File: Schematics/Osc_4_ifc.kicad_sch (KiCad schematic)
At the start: 34 parts, among them J35 Conn_01x10h, J37 Conn_01x12, J39 Conn_01x10h, J41 Conn_01x12, P2 Conn_01x03, U20 LM324, U85 LMT358N, U86 LM358, U87 LM358, U88 LMT358N, U97 LM78L05

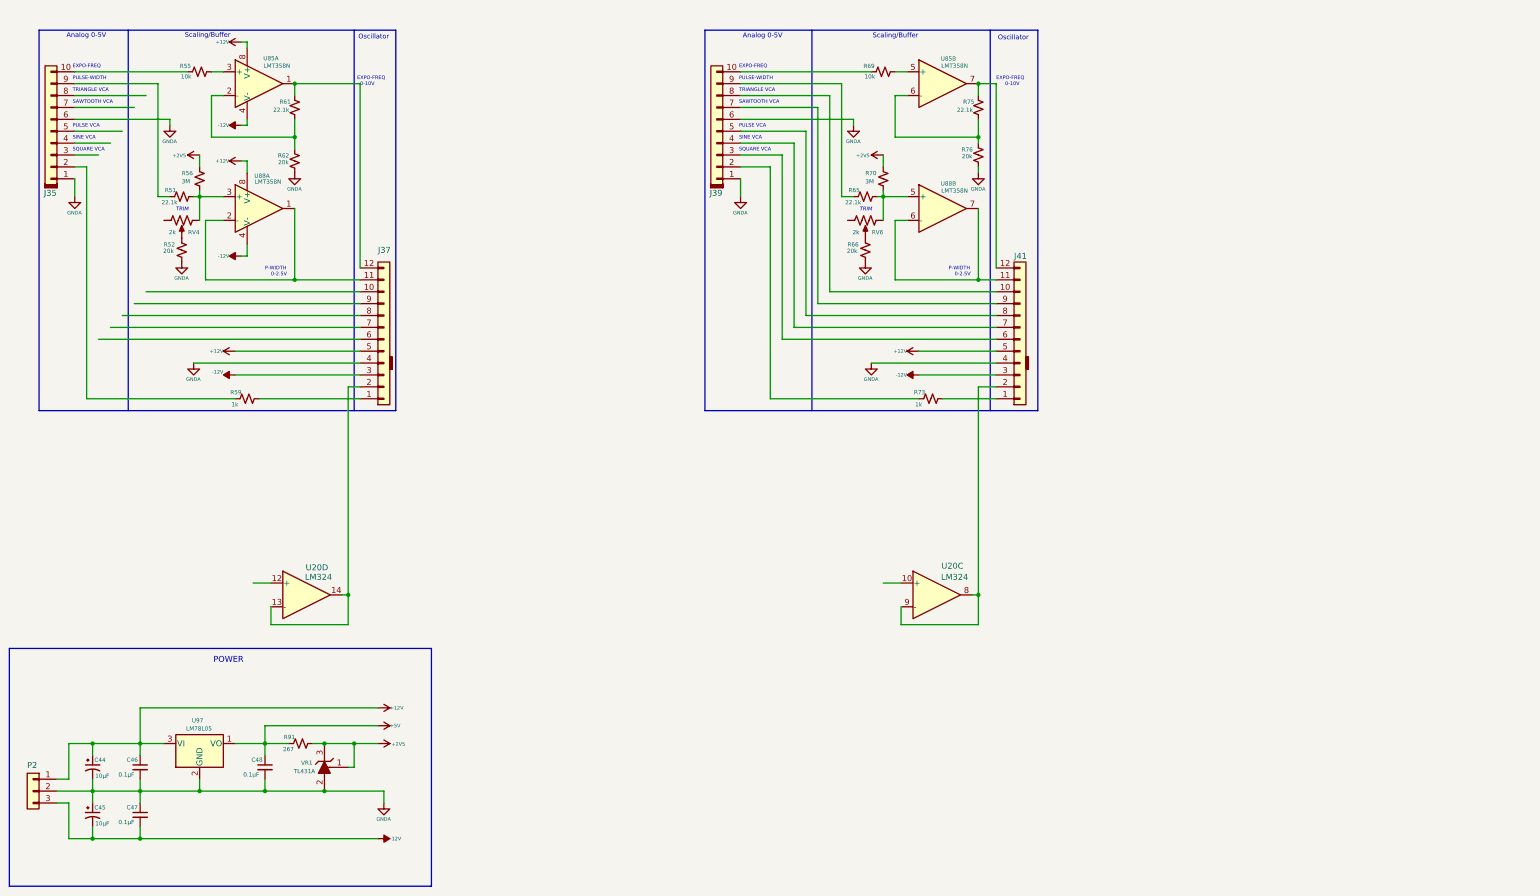
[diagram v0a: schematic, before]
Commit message: adding noise source and variable state filter.
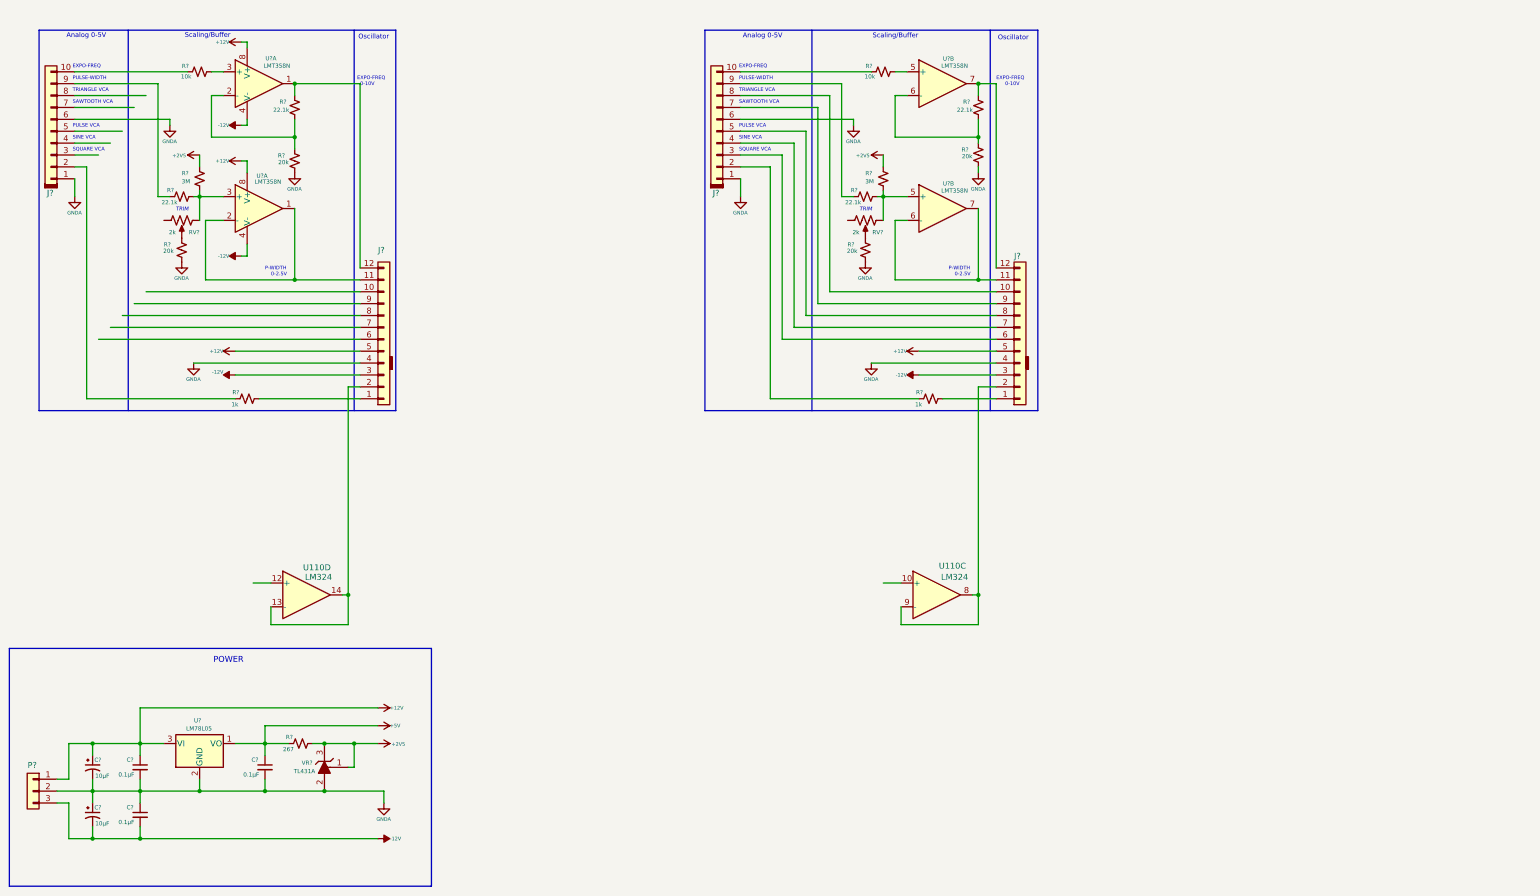
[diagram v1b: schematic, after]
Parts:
- renumbered C48 to C?, C46 to C?, C47 to C?, C45 to C?, C44 to C?, J39 to J?, J41 to J?, J37 to J?, J35 to J?, P2 to P?, R76 to R?, R70 to R?, R55 to R?, R59 to R?, R51 to R?, R66 to R?, R56 to R?, R73 to R?, R75 to R?, R91 to R?, R61 to R?, R65 to R?, R52 to R?, R69 to R?, R62 to R?, RV4 to RV?, RV6 to RV?, U20 to U110, U85 to U?, U87 to U?, U88 to U?, U86 to U?, U97 to U?, VR1 to VR?
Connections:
- net at RV?. (3): now also R?.1

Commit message: Noise boards added.
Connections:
- net at RV?. (3): now also R?.1

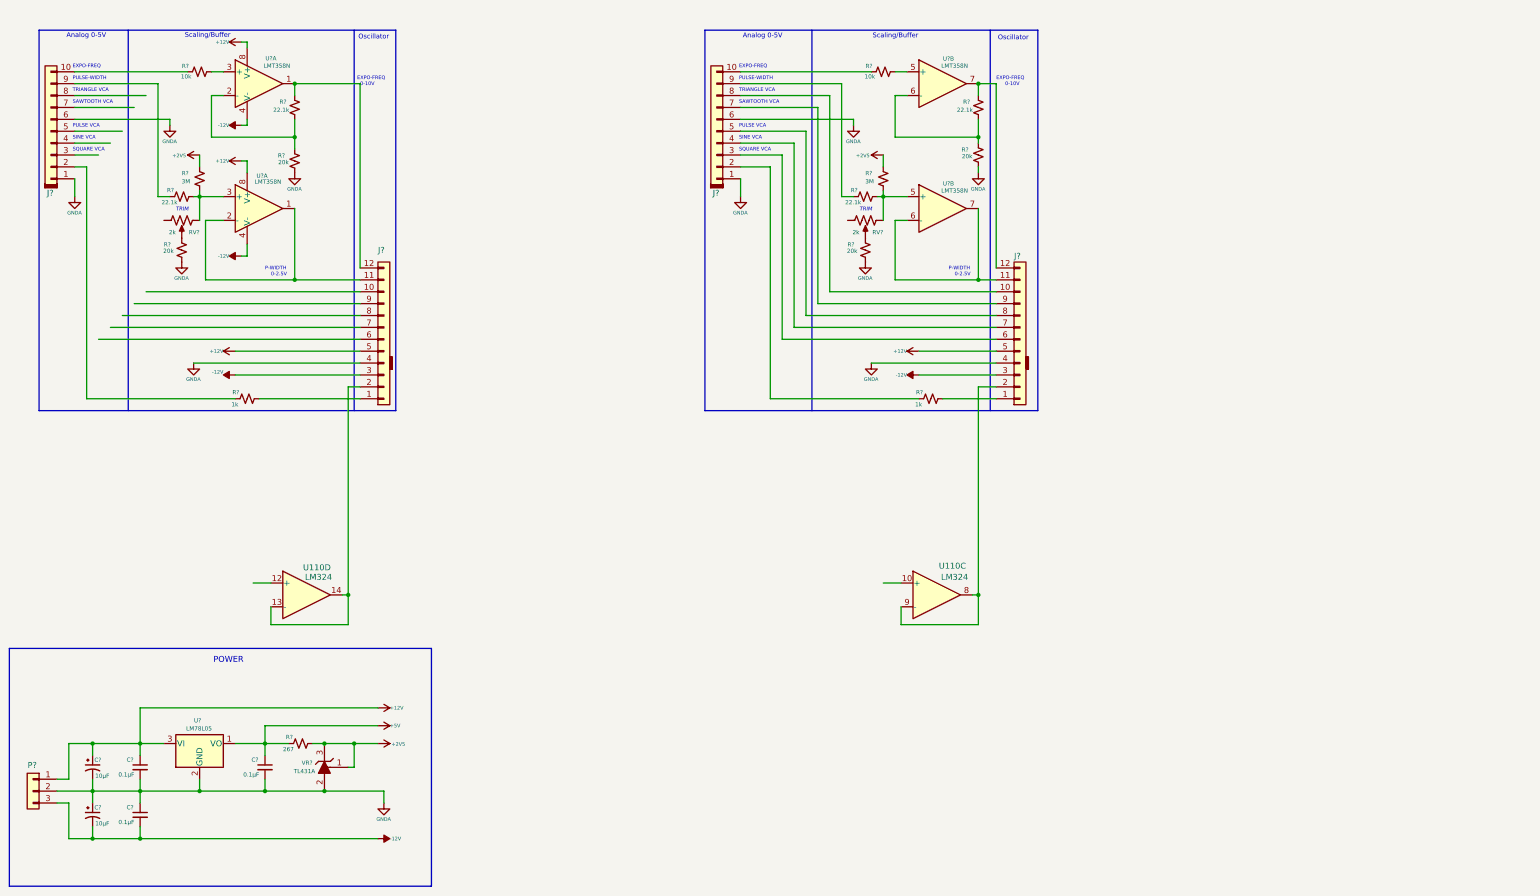
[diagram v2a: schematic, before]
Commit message: Update with noise filter & VCA as well as envelope generator software shell.
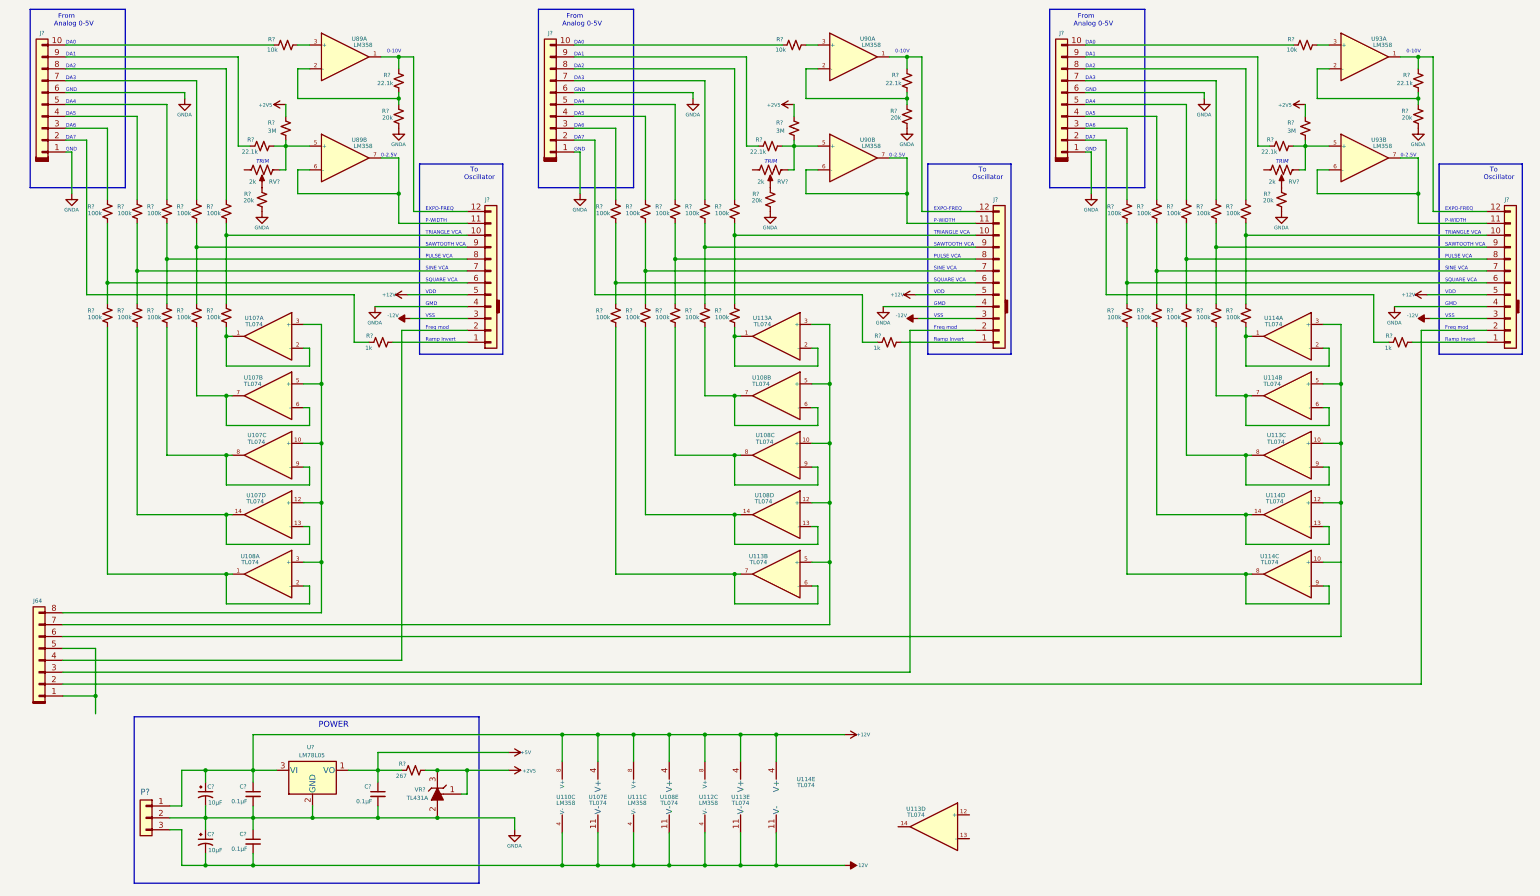
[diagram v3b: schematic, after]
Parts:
- removed J?: Conn_01x10h, symbol Connector_keyed_kicad_sym:Conn_01x10h
- removed J?: Conn_01x12, symbol Connector_keyed_kicad_sym:Conn_01x12
- removed R? (x2): 20k, symbol Device:R_Small_US
- removed R?: 3M, symbol Device:R_Small_US
- removed R?: 1k, symbol Device:R_Small_US
- removed R? (x2): 22.1k, symbol Device:R_Small_US
- removed R?: 10k, symbol Device:R_Small_US
- removed RV?: 2k, symbol Device:R_Potentiometer_US
- removed U110: LM324, symbol Amplifier_Operational:LM324
- removed U? (x4): LMT358N, symbol Amplifier_Operational:LM358
- removed U? (x2): LM358, symbol Amplifier_Operational:LM358
- added J64: Conn_01x08, symbol Connector_keyed_kicad_sym:Conn_01x08
- added J? (x2): Conn_01x10h, symbol Connector_keyed_kicad_sym:Conn_01x10h
- added J? (x2): Conn_01x12, symbol Connector_keyed_kicad_sym:Conn_01x12
- added R? (x30): 100k, symbol Device:R_Small_US
- added R? (x2): 10k, symbol Device:R_Small_US
- added R? (x4): 20k, symbol Device:R_Small_US
- added R? (x2): 3M, symbol Device:R_Small_US
- added R? (x4): 22.1k, symbol Device:R_Small_US
- added R? (x2): 1k, symbol Device:R_Small_US
- added RV? (x2): 2k, symbol Device:R_Potentiometer_US
- added U107, U108, U113, U114: TL074, symbol Amplifier_Operational:TL074
- added U110, U111, U112, U89, U90, U93: LM358, symbol Amplifier_Operational:LM358
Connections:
- net +12V: now also J?.5 (Pin_5), J?.5 (Pin_5), U107.4 (V+), U108.4 (V+), U110.8 (V+), U111.8 (V+), U112.8 (V+), U113.4 (V+), U114.4 (V+)
- net +2V5: now also R?.1, R?.1
- net -12V: now also J?.3 (Pin_3), J?.3 (Pin_3), U107.11 (V-), U108.11 (V-), U110.4 (V-), U111.4 (V-), U112.4 (V-), U113.11 (V-), U114.11 (V-)
- net GNDA: now also J?.1 (Pin_1), J?.1 (Pin_1), J?.4 (Pin_4), J?.4 (Pin_4), J?.6 (Pin_6), J?.6 (Pin_6), R?.2, R?.2, R?.2, R?.2
- net at R?.2: now also U89.3 (+)
- net at R?.2, R?.2, RV?. (3): now also U89.5 (+)
- net at RV?. (3): now also R?.1
- net at J?.12 (Pin_12), R?.1: now also U89.1
- net at R?.1, R?.2: now also U89.2 (-)
- net at J?.2 (Pin_2): now also J64.4 (Pin_4)
- net at J?.11 (Pin_11): now also U89.6 (-), U89.7
- net at J?.10 (Pin_10): now also R?.1, R?.2
- net at J?.6 (Pin_6): now also R?.1, R?.2
- net at J?.7 (Pin_7): now also R?.1, R?.2
- net at J?.8 (Pin_8): now also R?.1, R?.2
- net at J?.9 (Pin_9): now also R?.1, R?.2
- net at J?.3 (Pin_3): now also R?.1
- net at J?.4 (Pin_4): now also R?.1
- net at J?.5 (Pin_5): now also R?.1
- net at J?.7 (Pin_7): now also R?.1
- net at J?.8 (Pin_8): now also R?.1
- new net: J?.5 (Pin_5), R?.1 (x2)
- new net: J?.8 (Pin_8), R?.1, R?.2 (x2)
- new net: J?.10 (Pin_10), R?.1, R?.2 (x2)
- new net: R?.2, U114.1, U114.2 (-)
- new net: J64.8 (Pin_8), U107.10 (+), U107.12 (+), U107.3 (+), U107.5 (+), U108.3 (+)
- new net: R?.2, U107.13 (-), U107.14
- new net: R?.2, U114.8, U114.9 (-)
- new net: J?.10 (Pin_10), R?.1 (x2)
- new net: R?.2, U90.3 (+)
- new net: R?.2, R?.2, RV?. (3), U93.5 (+)
- new net: J?.11 (Pin_11), U93.6 (-), U93.7
- new net: J64.6 (Pin_6), U113.10 (+), U114.12 (+), U114.3 (+), U114.5 (+)
- new net: R?.2, U113.8, U113.9 (-)
- new net: J?.7 (Pin_7), R?.1, R?.2 (x2)
- new net: R?.2, U114.13 (-), U114.14
- new net: J?.3 (Pin_3), R?.1 (x2)
- new net: J?.6 (Pin_6), R?.1, R?.2 (x2)
- new net: R?.2, U108.13 (-), U108.14
- new net: J64.7 (Pin_7), U108.10 (+), U108.12 (+), U108.5 (+), U113.3 (+), U113.5 (+)
- new net: J?.4 (Pin_4), R?.1 (x2)
- new net: J?.2 (Pin_2), R?.1 (x2)
- new net: J?.7 (Pin_7), R?.1 (x2)
- new net: J?.8 (Pin_8), R?.1 (x2)
- new net: J?.9 (Pin_9), R?.1 (x2)
- new net: R?.2, U107.8, U107.9 (-)
- new net: R?.2, U108.1, U108.2 (-)
- new net: R?.1, R?.2, U90.2 (-)
- new net: J?.12 (Pin_12), R?.1, U93.1
- new net: R?.1, R?.2, U93.2 (-)
- new net: R?.2, U93.3 (+)
- new net: R?.2, U108.8, U108.9 (-)
- new net: R?.2, U108.6 (-), U108.7
- new net: R?.2, U114.6 (-), U114.7
- new net: R?.2, U113.6 (-), U113.7
- new net: R?.2, R?.2, RV?. (3), U90.5 (+)
- new net: R?.1, RV?. (3) (x2)
- new net: J?.9 (Pin_9), R?.1, R?.2 (x2)
- new net: R?.2, U107.6 (-), U107.7
- new net: J?.1 (Pin_1), R?.2 (x2)
- new net: J64.2 (Pin_2), J?.2 (Pin_2)
- new net: R?.2, U113.1, U113.2 (-)
- new net: J?.12 (Pin_12), R?.1, U90.1
- new net: J?.11 (Pin_11), U90.6 (-), U90.7
- new net: R?.2, U107.1, U107.2 (-)
- new net: J64.3 (Pin_3), J?.2 (Pin_2)
- new net: J64.1 (Pin_1), J64.5 (Pin_5)
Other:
- note added: "DA0"
- note added: "DA1"
- note added: "DA2"
- note added: "DA3"
- note added: "DA4"
- note added: "DA5"
- note added: "DA6"
- note added: "DA7"
- note added: "Freq mod"
- note added: "From Analog 0-5V"
- note added: "GMD"
- note added: "GND"
- note added: "Ramp Invert"
- note added: "To Oscillator"
- note added: "VDD"
- note added: "VSS"
- note removed: "Analog 0-5V"
- note removed: "Oscillator"
- note removed: "PULSE-WIDTH"
- note removed: "Scaling/Buffer"
- moved on the sheet: C?, J?, P?, R?, RV?, U?, VR?

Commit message: sync up first noise board.
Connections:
- net at RV?. (3): now also R?.1

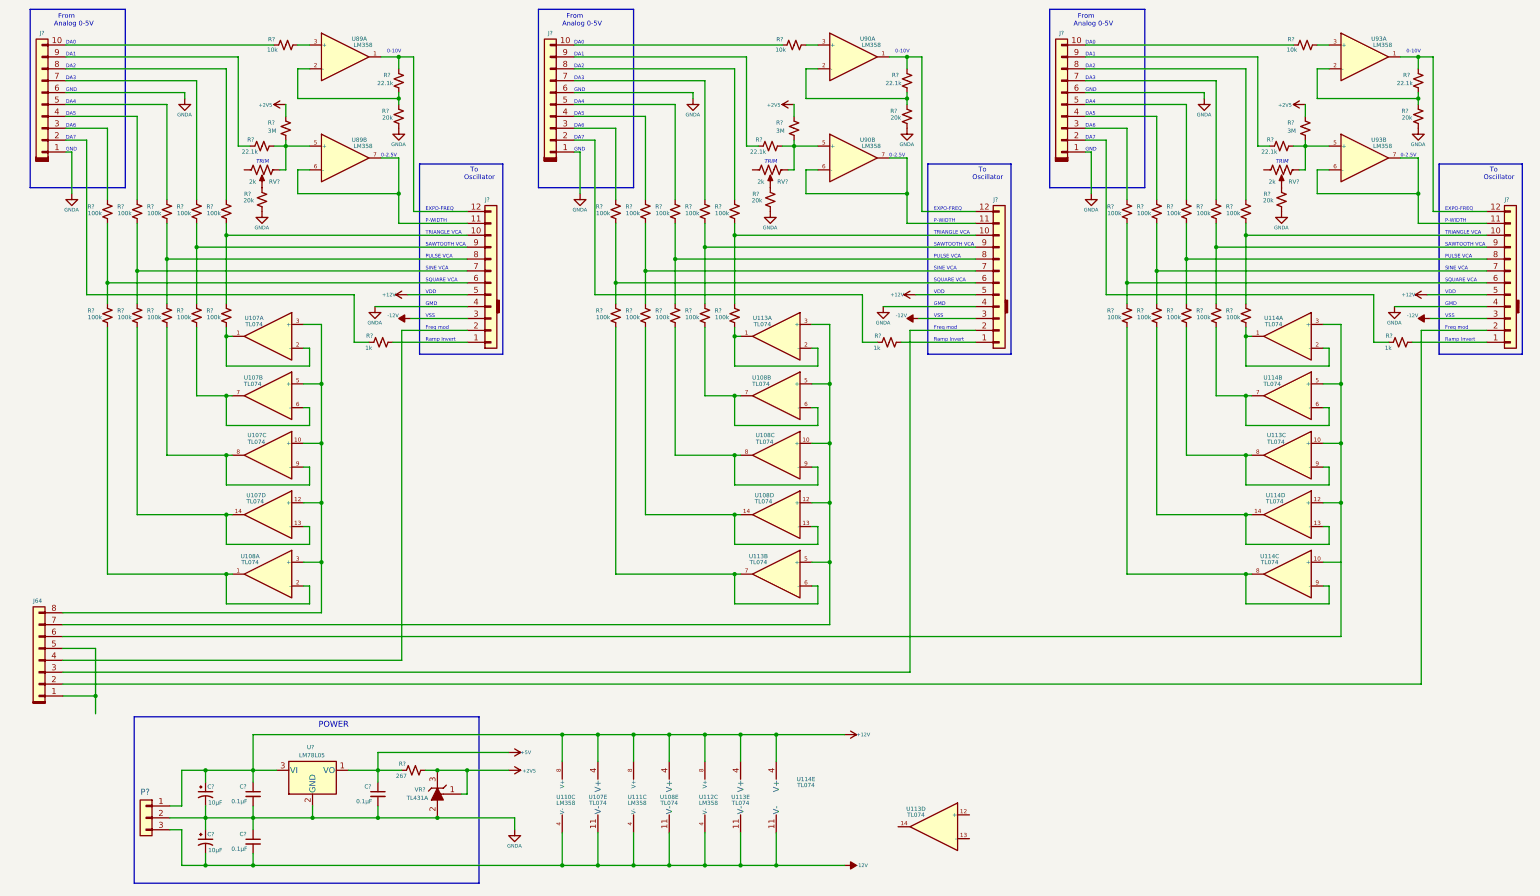
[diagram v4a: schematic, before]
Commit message: Partial software with complete hardware on best 3 state filter with 4 outputs.
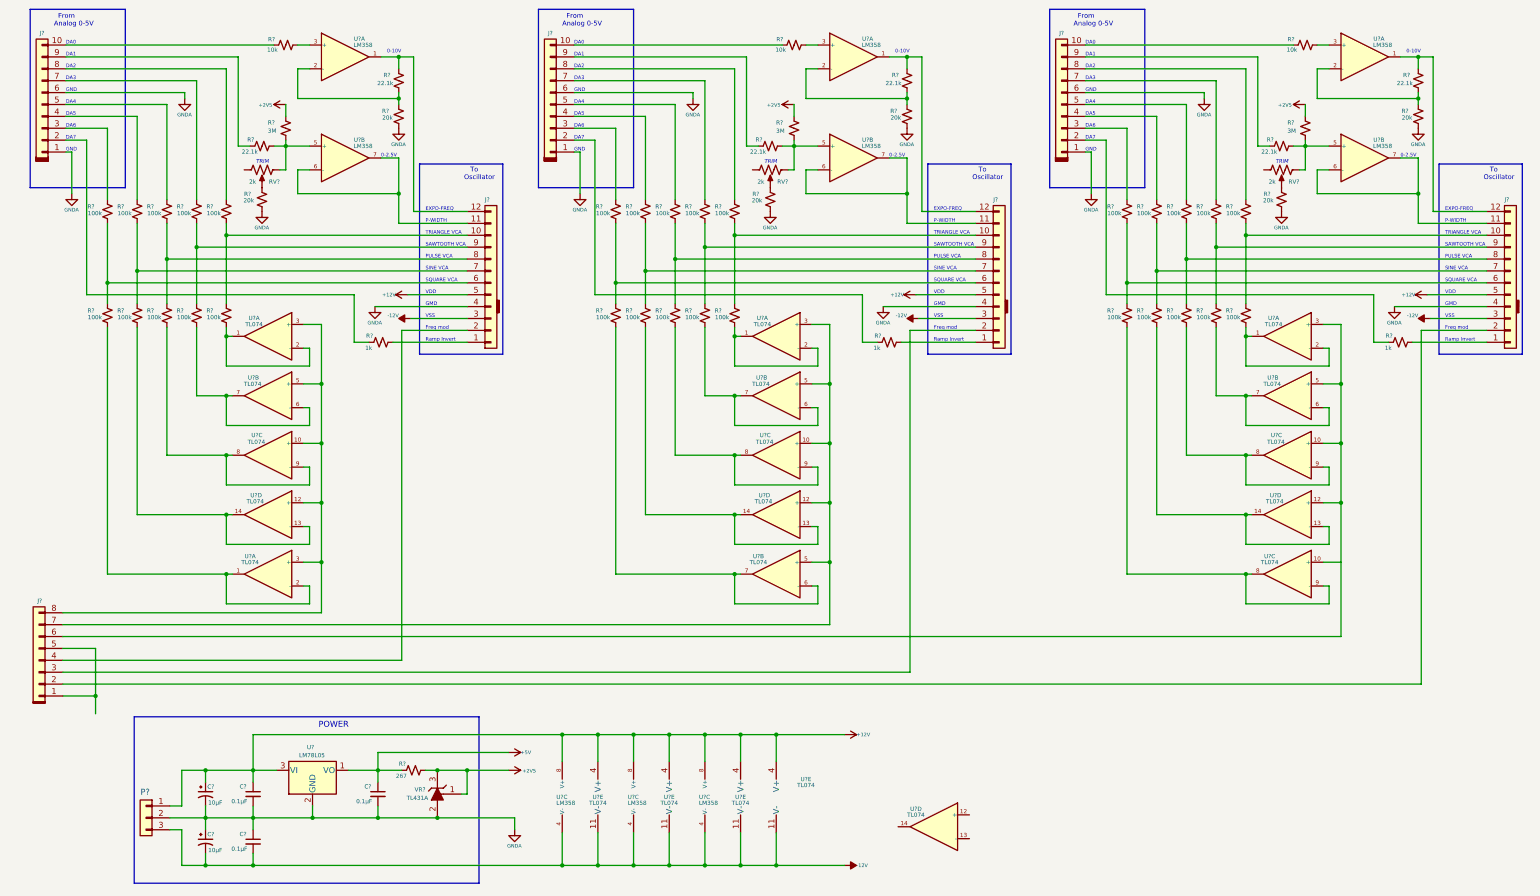
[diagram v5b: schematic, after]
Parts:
- renumbered J64 to J?, U107 to U?, U114 to U?, U93 to U?, U113 to U?, U108 to U?, U112 to U?, U111 to U?, U110 to U?, U89 to U?, U90 to U?
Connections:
- net at RV?. (3): now also R?.1

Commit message: - Updated current libraries - New 7 inc display with ESP32S3 and second USB upload port - Start of I2C feeder interface slave on display.
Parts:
- gave numbers to parts that had none: 81
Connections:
- net at RV26. (3): now also R356.1
